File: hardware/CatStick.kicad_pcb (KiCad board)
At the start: 4 copper layers, 81 x 20 mm, 85 parts, among them J1 Antenna, J2 Conn_01x06_Female, J3 JTAG, P1 USB_C_Plug_USB2.0, SW1 SW, U1 AP2112K-3.3, U2 RFSW8006QTR7, U3 ATSAMD21E18A, U4 0900PC15A0036, U5 0900FM15D0039, U6 SW409, U7 SX1262IMLTRT, U8 CC1352R1F3RGZR, Y1 48MHz, Y2 32.768kHz, Y3 32Mhz_10pF_10ppm

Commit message: updatePCB
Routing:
- net +3V3: track 23.9 -> 29.7 mm
- net GND: track 136.8 -> 138.1 mm

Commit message: updateTraces
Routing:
- net /LED3: track 15.1 -> 11.4 mm
- net /U_SWITCH: track 11.0 -> 10.3 mm
- net /SWDIO: track 19.8 -> 19.1 mm
- net /SWCLK: track 18.5 -> 17.9 mm
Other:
- board text added: "Impedancias: USBC(D-,D+) = 90 ohm (0.2032)"
- board text removed: "Impedancias: D+,D- = 90 ohm (0.2032)"

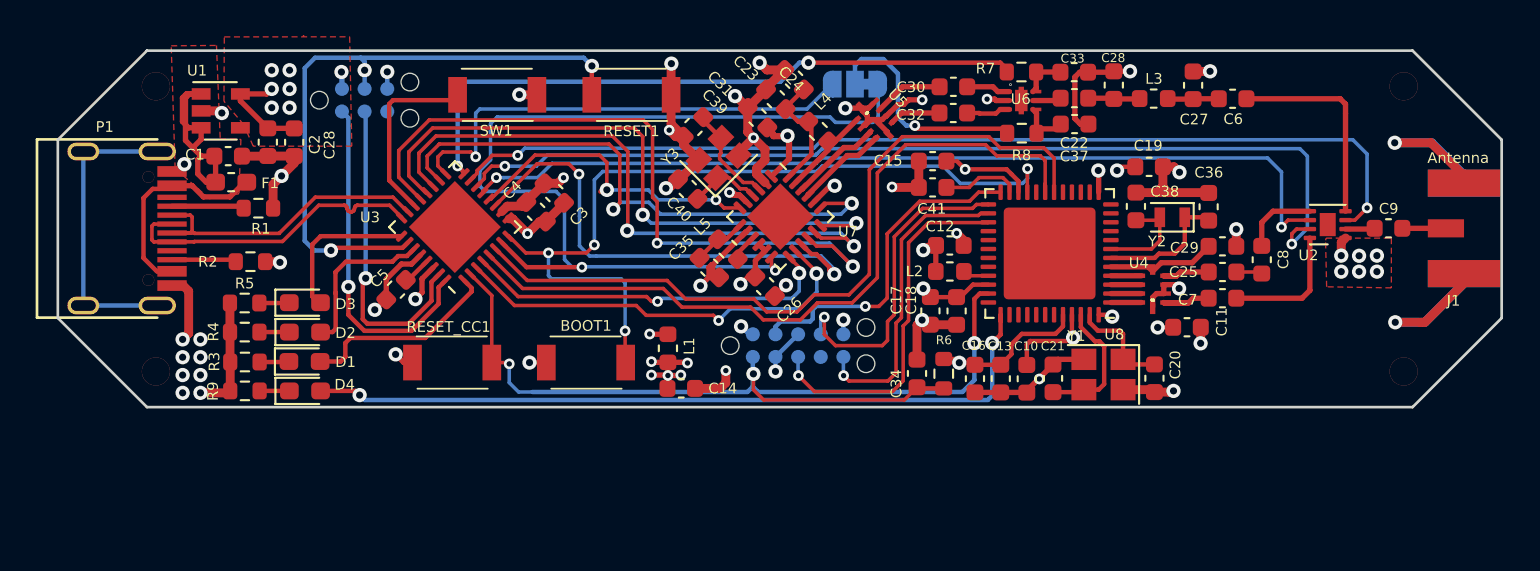
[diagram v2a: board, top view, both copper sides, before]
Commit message: update RF with correct impedance
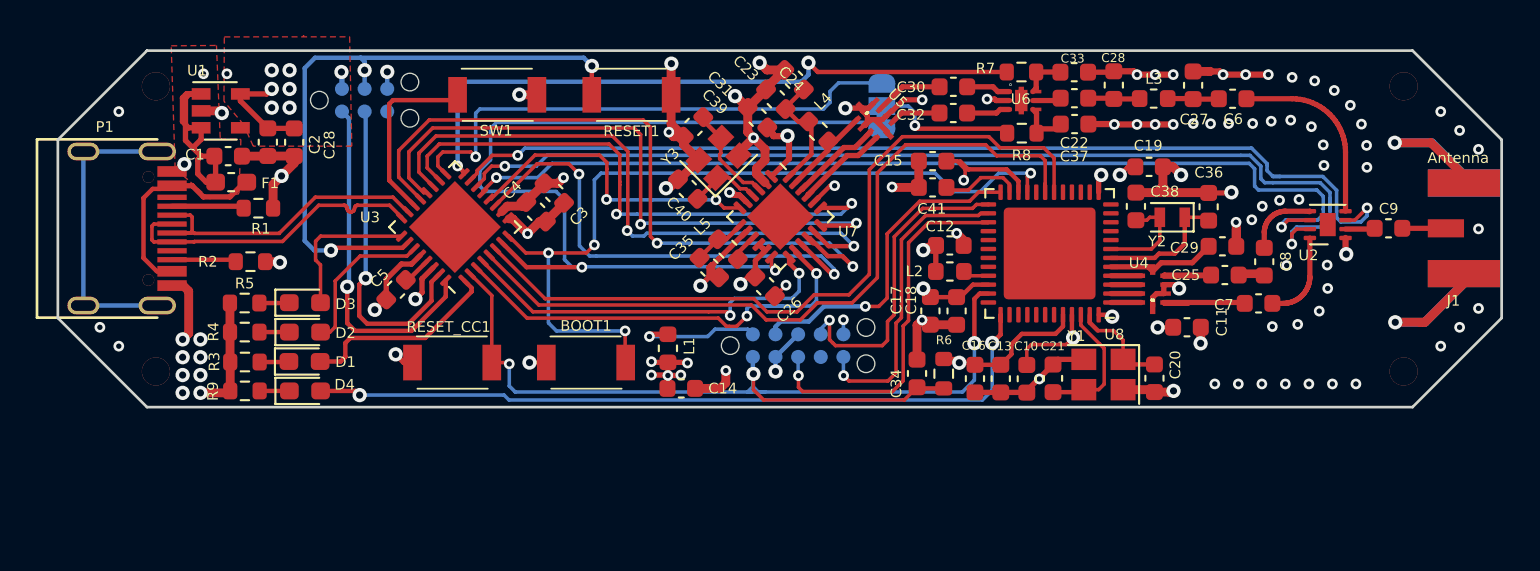
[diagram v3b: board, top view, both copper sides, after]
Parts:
- moved C7 2.05 mm to (152.4, 114.2)
- moved JP1 1.95 mm to (131.2, 103.1), turned to 90 degrees
- moved C25 0.21 mm to (150.5, 112.6)
- moved C8 0.18 mm to (152.7, 111.8)
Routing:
- net GND: track 138.0 -> 149.1 mm, vias 47 -> 101
- net /VDDS: track 77.7 -> 83.6 mm
- net Net-(JP1-Pad2): track 12.9 -> 8.07 mm
- net /CTF3: track 50.8 -> 54.7 mm
- net /UBP_2_4_GHZ: track 4.02 -> 7.34 mm
- net /DIO22: track 26.6 -> 29.8 mm
- net /DIO2: track 54.3 -> 51.9 mm
- net Net-(C25-Pad2): track 3.64 -> 5.98 mm
- net /CTF2: track 54.8 -> 57.1 mm
- net Net-(C7-Pad2): track 7.25 -> 5.13 mm
- net /BUSY: track 23.8 -> 25.6 mm
- net /RESET_CC: track 53.6 -> 55.2 mm
- net /UBP_SUB-1_GHZ: track 1.46 -> 2.91 mm
- net Net-(C6-Pad2): track 11.7 -> 10.6 mm
- net /DIO1: track 21.1 -> 22.2 mm
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
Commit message: update impedance information
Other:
- board text added: "Impedance: USBC(D-,D+) = 90 ohm (0.2032 mm) RF = 50 Ohms (0.293 mm) Stackup JLC7628"
- board text removed: "Impedancias: USBC(D-,D+) = 90 ohm (0.2032)"

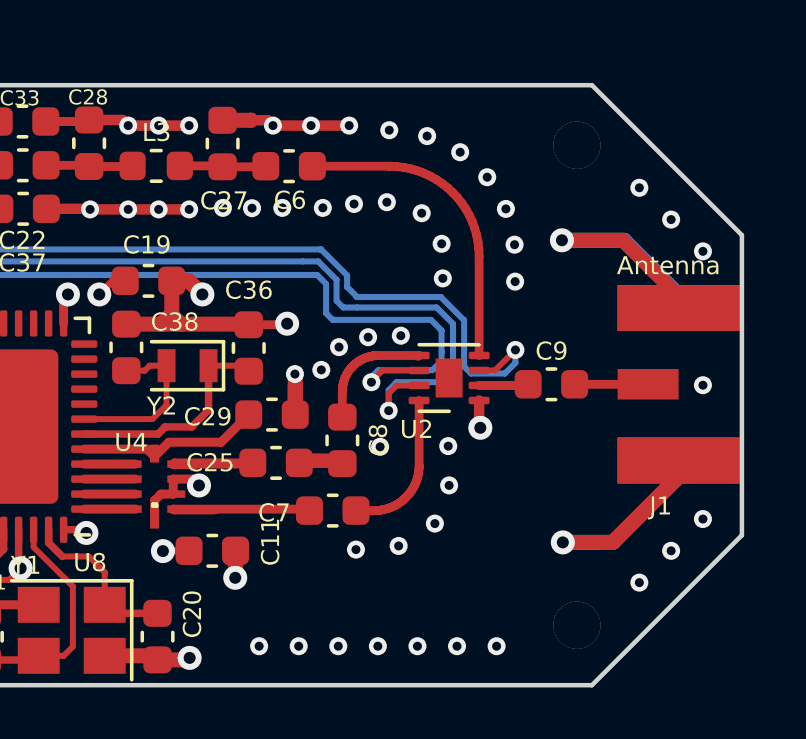
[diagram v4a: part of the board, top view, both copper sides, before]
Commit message: update RF traces
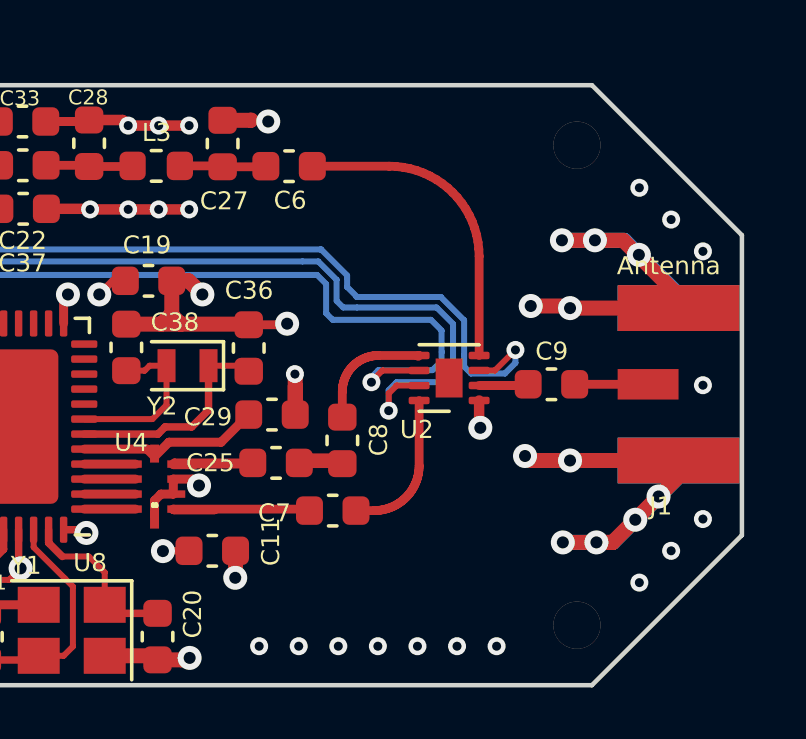
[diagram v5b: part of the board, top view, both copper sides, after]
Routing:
- net GND: track 149.1 -> 157.4 mm, vias 101 -> 82

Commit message: NRoutingCC13inProgress
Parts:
- removed the C20 at (146.5, 118.4)
- removed the C21 at (140.8, 118.4)
- removed the C28 at (98.3, 105.1)
- removed the C38 at (145.5, 108.7)
- removed C41: 1uF, Capacitor_SMD:C_0603_1608Metric
- added C32: 0.1uF, Capacitor_SMD:C_0603_1608Metric, F.Cu at (138.4, 118.4)
- added C39: 1uF, Capacitor_SMD:C_0603_1608Metric, F.Cu at (134.9, 107.2)
- C10: value 22uF -> 0.1uF
- C11, C12, C16, C2: value 100nF -> 0.1uF
- C13, C15: value 12pF -> 0.1uF
- C14, C17: value 100nF -> 22uF
- C18: value 22uF -> 22pF
- C19: value 100nF -> 22pF
- C24: renamed from C26; value 100nF -> 0.1uF
- C34: value 100nF -> 10pF
- C36: value 12pF -> 10pF
- C37: renamed from C40; value 18pF -> 12pF
- C38: renamed from C39; value 18pF -> 12pF
- F1: footprint Fuse:Fuse_0603_1608Metric_Pad1.05x0.95mm_HandSolder -> Fuse:Fuse_0805_2012Metric_Pad1.15x1.40mm_HandSolder
- J3: value JTAG -> Conn_01x06_Female; footprint Connector:Tag-Connect_TC2050-IDC-NL_2x05_P1.27mm_Vertical -> Connector:Tag-Connect_TC2030-IDC-NL_2x03_P1.27mm_Vertical
- Y3: value 32Mhz_10pF_10ppm -> 32Mhz
- moved C34 19.2 mm to (150.0, 108.8)
- moved C14 15.6 mm to (134.7, 113.7), turned to 180 degrees
- moved L1 15.6 mm to (134.8, 117.7), turned to 180 degrees
- moved C15 14.6 mm to (142.0, 118.4), turned to 270 degrees
- moved C18 14.3 mm to (149.2, 118.4)
- moved C11 14.1 mm to (137.8, 106.1), turned to 180 degrees
- moved C10 12.8 mm to (144.2, 106.5), turned to 0 degrees
- moved C19 12.2 mm to (143.5, 118.4), turned to 90 degrees
- moved C16 10.6 mm to (146.6, 115.7), turned to 0 degrees
- moved C12 9.29 mm to (140.6, 118.4), turned to 270 degrees
- moved C13 4.53 mm to (134.7, 115.2), turned to 180 degrees
- moved C36 3.64 mm to (145.9, 108.8)
- moved C37 3.52 mm to (120.6, 104.3), turned to 225 degrees
- moved C38 3.31 mm to (120.1, 107.5), turned to 135 degrees
- moved Y1 2.68 mm to (146.3, 118.2)
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- renumbered C22 to C20, C23 to C21, C24 to C22, C25 to C23, C27 to C25, C28 to C26, C29 to C27, C30 to C28, C31 to C29, C32 to C30, C33 to C31, C35 to C33, C37 to C35
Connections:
- net /JTAG_TCKC renamed /cJTAG_TCK
- net /JTAG_TMSC renamed /cJTAG_TMSC
- C10 pad 1: /VDDR -> /VDDS
- C11 pad 1: /VDDR -> /VDDS
- C12 pad 1: /VDDR -> /VDDS
- C15 pad 1: /VDDS -> Net-(C15-Pad1)
- C16 pad 1: /VDDS -> Net-(C15-Pad1)
- C17 pad 1: /VDDS -> Net-(C15-Pad1)
- C18 pad 1: /VDDS -> /X48M_P
- C19 pad 1: /VDDS -> /X48M_N
- C34 pad 1: /RESET_CC -> Net-(C34-Pad1)
- C37 pad 1: Net-(C40-Pad1) -> /XTA
- C38 pad 1: Net-(C39-Pad1) (its old number) -> /XTB
- J3 pad 3: GND -> /RESET_CC
- J3 pad 6: /JTAG_TDO -> Net-(J3-Pad6)
- L2 pad 2: /VDDR -> Net-(C15-Pad1)
- U7 pad 3: Net-(C39-Pad1) (its old number) -> /XTA
- U7 pad 4: Net-(C40-Pad1) -> /XTB
- U8 pad 26: /JTAG_TDO -> Net-(U8-Pad26)
- U8 pad 27: /JTAG_TDI -> Net-(U8-Pad27)
- U8 pad 6: Net-(C36-Pad1) -> Net-(C34-Pad1)
- U8 pad 7: Net-(C38-Pad1) -> Net-(C36-Pad1)
- Y2 pad 1: Net-(C36-Pad1) -> Net-(C34-Pad1)
- Y2 pad 2: Net-(C38-Pad1) -> Net-(C36-Pad1)
- Y3 pad 1: Net-(C40-Pad1) -> /XTB
- Y3 pad 3: Net-(C39-Pad1) (its old number) -> /XTA
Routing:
- net /VDDS: track 83.6 -> 0.00 mm, vias 10 -> 0
- net /RESET_CC: track 55.2 -> 8.19 mm, vias 3 -> 1
- net /TXD: track 42.8 -> 0.00 mm
- net /RXD: track 42.7 -> 0.00 mm
- net GND: track 157.4 -> 123.2 mm, vias 82 -> 68
- net /LED4: track 42.9 -> 10.8 mm, vias 2 -> 1
- net /VDDR: track 30.0 -> 0.00 mm, vias 4 -> 0
- net /JTAG_TDI: track 20.8 -> 0.00 mm, vias 1 -> 0
- net /cJTAG_TMSC: track 18.3 -> 0.00 mm, vias 1 -> 0
- net /cJTAG_TCK: track 17.6 -> 0.00 mm, vias 1 -> 0
- net /JTAG_TDO: track 17.4 -> 0.00 mm, vias 1 -> 0
- net /X48M_N: track 7.49 -> 0.00 mm
- net Net-(C36-Pad1): track 7.37 -> 0.00 mm
- net /BOOT: track 45.9 -> 38.5 mm, vias 4 -> 3
- net VCC: track 14.1 -> 21.4 mm
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
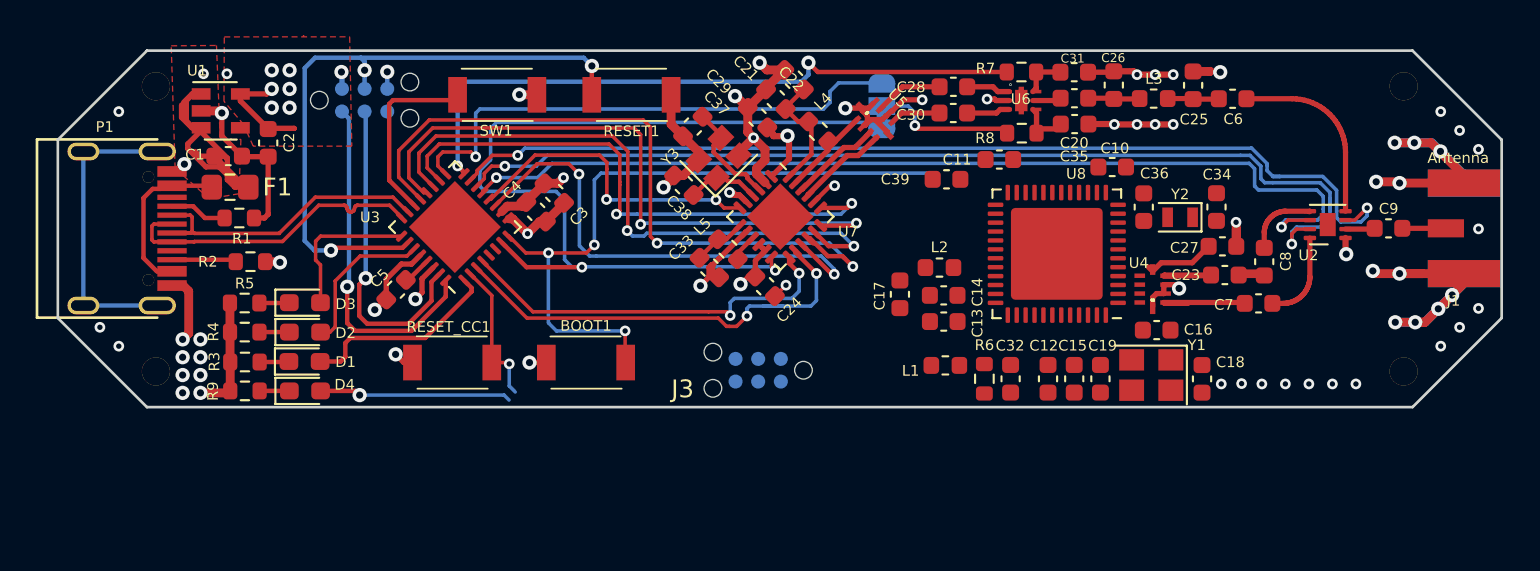
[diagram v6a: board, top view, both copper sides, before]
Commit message: changeCap0402
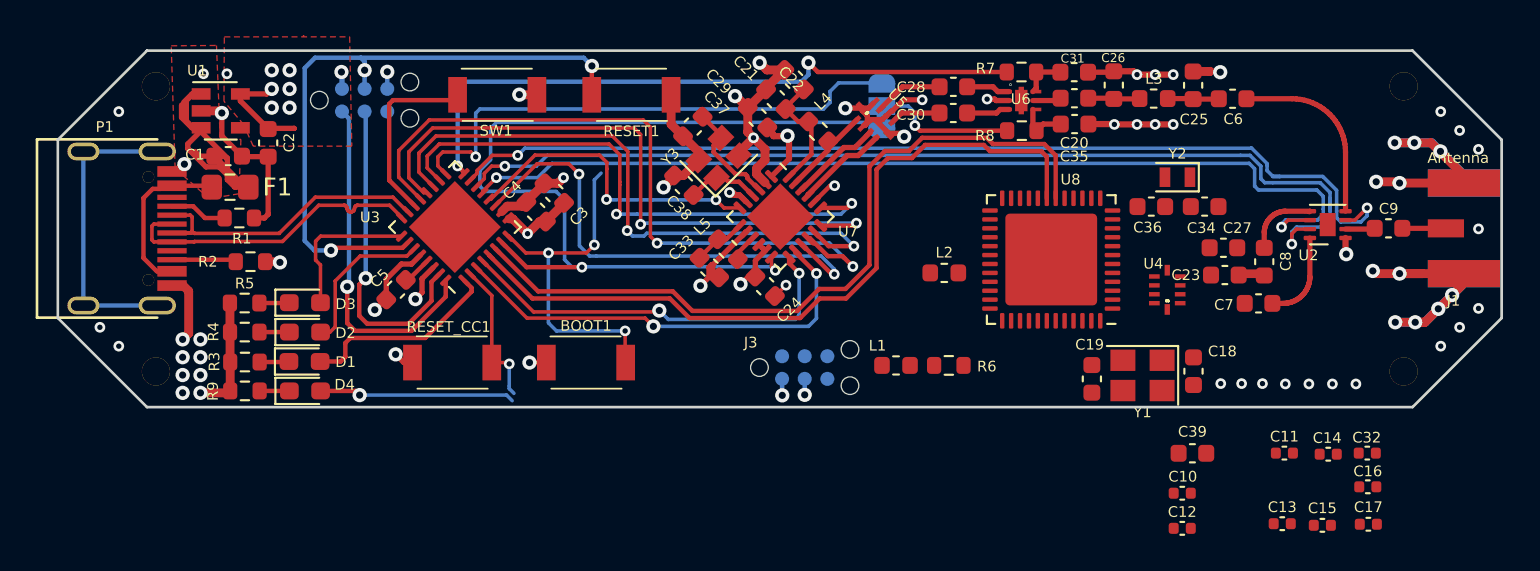
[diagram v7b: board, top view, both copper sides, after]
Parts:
- C10, C11, C12, C13, C15, C16, C32: value 0.1uF -> 100nF; footprint Capacitor_SMD:C_0603_1608Metric -> Capacitor_SMD:C_0402_1005Metric
- C14, C17: footprint Capacitor_SMD:C_0603_1608Metric -> Capacitor_SMD:C_0402_1005Metric
- moved C17 29.3 mm to (158.5, 126.6), turned to 0 degrees
- moved C14 23.3 mm to (156.3, 122.6), turned to 0 degrees
- moved C11 23.0 mm to (153.8, 122.6), turned to 0 degrees
- moved C13 22.1 mm to (153.7, 126.5), turned to 0 degrees
- moved C39 20.7 mm to (148.7, 122.6), turned to 0 degrees
- moved C32 20.4 mm to (158.5, 122.6), turned to 0 degrees
- moved C10 18.7 mm to (148.1, 124.8)
- moved C15 16.2 mm to (155.9, 126.6), turned to 0 degrees
- moved C16 14.8 mm to (158.5, 124.5)
- moved C12 11.3 mm to (148.1, 126.8), turned to 0 degrees
- moved L1 2.77 mm to (132.0, 117.7)
- moved J3 2.61 mm to (126.9, 117.8), turned to 0 degrees
- moved Y2 2.25 mm to (147.8, 107.1)
- moved R6 2.13 mm to (135.0, 117.7), turned to 180 degrees
- moved U4 0.82 mm to (147.2, 112.4)
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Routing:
- net /RXD: track 0.00 -> 42.9 mm
- net /TXD: track 0.00 -> 42.6 mm
- net /BOOT: track 38.5 -> 19.8 mm
- net /UBP_2_4_GHZ: track 7.34 -> 0.01 mm
- net Net-(C23-Pad2): track 5.98 -> 0.00 mm
- net /RX_TX: track 4.07 -> 0.00 mm
- net GND: track 123.2 -> 119.3 mm, vias 68 -> 67
- net /cJTAG_TMSC: track 0.00 -> 0.93 mm, vias 0 -> 1
- net /cJTAG_TCK: track 0.00 -> 0.89 mm, vias 0 -> 1
- net /BUSY: track 25.6 -> 24.9 mm
- net /DIO1: track 22.2 -> 22.8 mm
- removed copper zone on VCC, net +3V3
- removed copper zone on GND, net GND

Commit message: changeLabelsSize
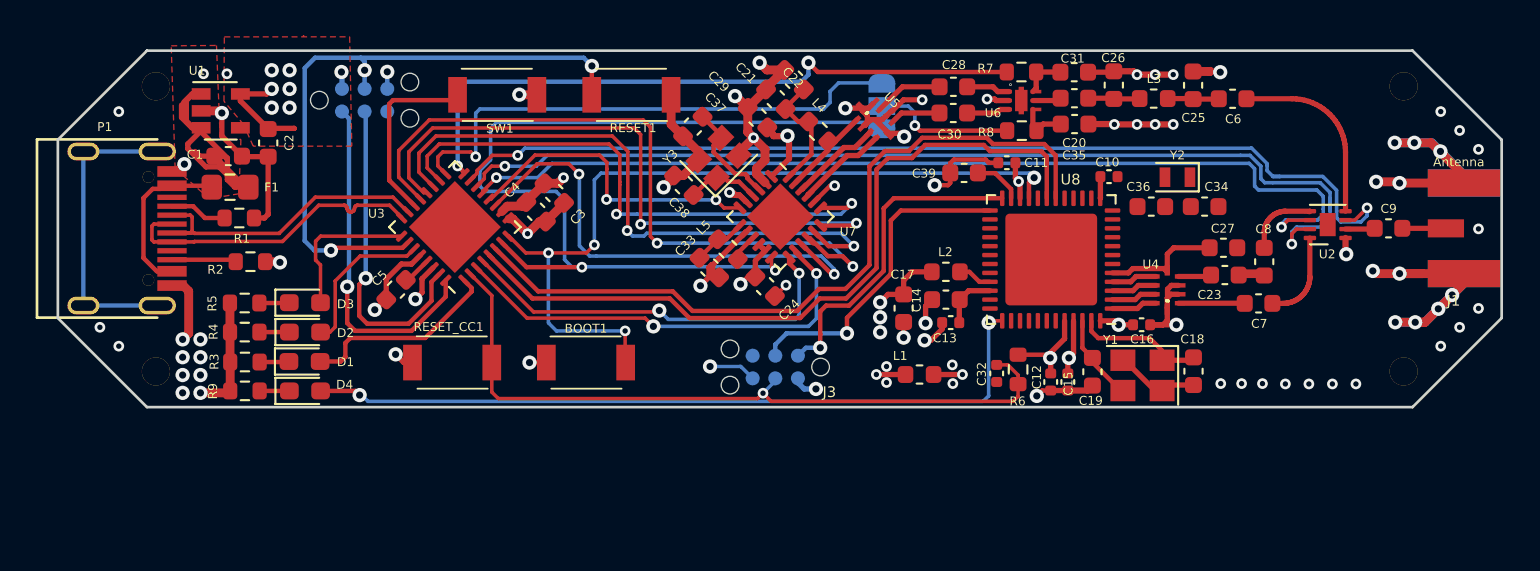
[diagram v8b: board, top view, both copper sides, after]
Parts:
- C14, C17: footprint Capacitor_SMD:C_0402_1005Metric -> Capacitor_SMD:C_0603_1608Metric
- moved C17 28.7 mm to (132.4, 114.5), turned to 270 degrees
- moved C14 23.1 mm to (134.8, 114.0), turned to 180 degrees
- moved C11 22.5 mm to (138.2, 106.3), turned to 180 degrees
- moved C13 21.8 mm to (135.1, 115.3), turned to 180 degrees
- moved C32 21.3 mm to (137.7, 118.1), turned to 270 degrees
- moved C39 20.3 mm to (135.8, 106.9), turned to 180 degrees
- moved C10 18.2 mm to (144.0, 107.1)
- moved C15 16.4 mm to (141.7, 118.6), turned to 270 degrees
- moved C16 15.6 mm to (145.8, 115.4)
- moved C12 11.0 mm to (140.7, 118.6), turned to 270 degrees
- moved R6 3.89 mm to (138.9, 117.9), turned to 90 degrees
- moved J3 1.65 mm to (125.2, 117.8), turned to 180 degrees
- moved L1 1.42 mm to (133.3, 118.2)
- moved C19 0.40 mm to (143.0, 118.0), turned to 270 degrees
- moved L2 0.11 mm to (134.8, 112.4)
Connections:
- C15 pad 1: Net-(C15-Pad1) -> /VDDR
- C16 pad 1: Net-(C15-Pad1) -> /VDDR
- C17 pad 1: Net-(C15-Pad1) -> /VDDR
- L2 pad 2: Net-(C15-Pad1) -> /VDDR
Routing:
- net /RESET_CC: track 8.24 -> 41.9 mm
- net /LED4: track 11.0 -> 42.8 mm, vias 1 -> 2
- net GND: track 119.3 -> 145.0 mm, vias 67 -> 74
- net /BOOT: track 19.8 -> 45.5 mm, vias 3 -> 4
- net /cJTAG_TMSC: track 0.93 -> 18.4 mm
- net /cJTAG_TCK: track 0.89 -> 18.0 mm
- net /VDDS: track 0.00 -> 13.3 mm, vias 0 -> 5
- net /VDDR: track 0.00 -> 9.09 mm, vias 0 -> 5
- net /X48M_P: track 0.00 -> 7.37 mm
- net /RX_TX: track 0.00 -> 6.78 mm
- net /X48M_N: track 0.00 -> 5.09 mm
- net /UBP_2_4_GHZ: track 0.01 -> 3.72 mm
- net +3V3: track 21.9 -> 24.9 mm, vias 12 -> 16
- net Net-(C39-Pad1): track 0.00 -> 2.75 mm
- net /SUB_1_GHZ_RF_P: track 0.00 -> 2.57 mm
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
